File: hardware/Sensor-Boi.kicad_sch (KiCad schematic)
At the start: 3 parts, among them U1 ESP32-S3-WROOM-1, U2 MAX31856, U3 SN65HVD230

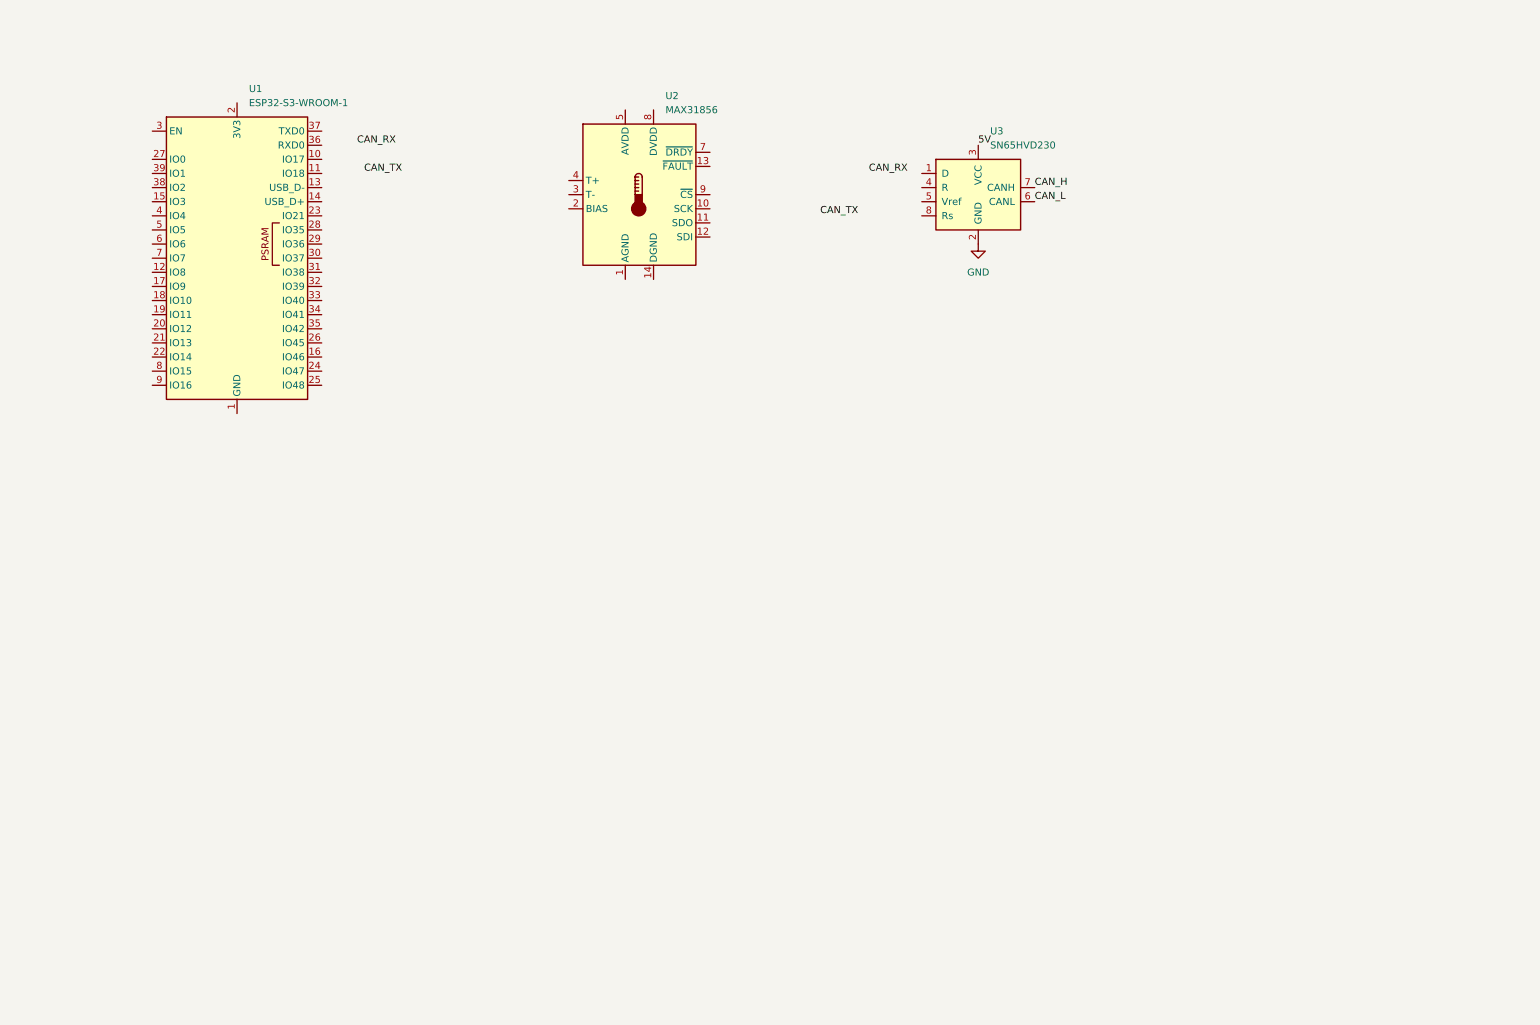
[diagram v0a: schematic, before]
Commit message: add a majority of symbols to schematic
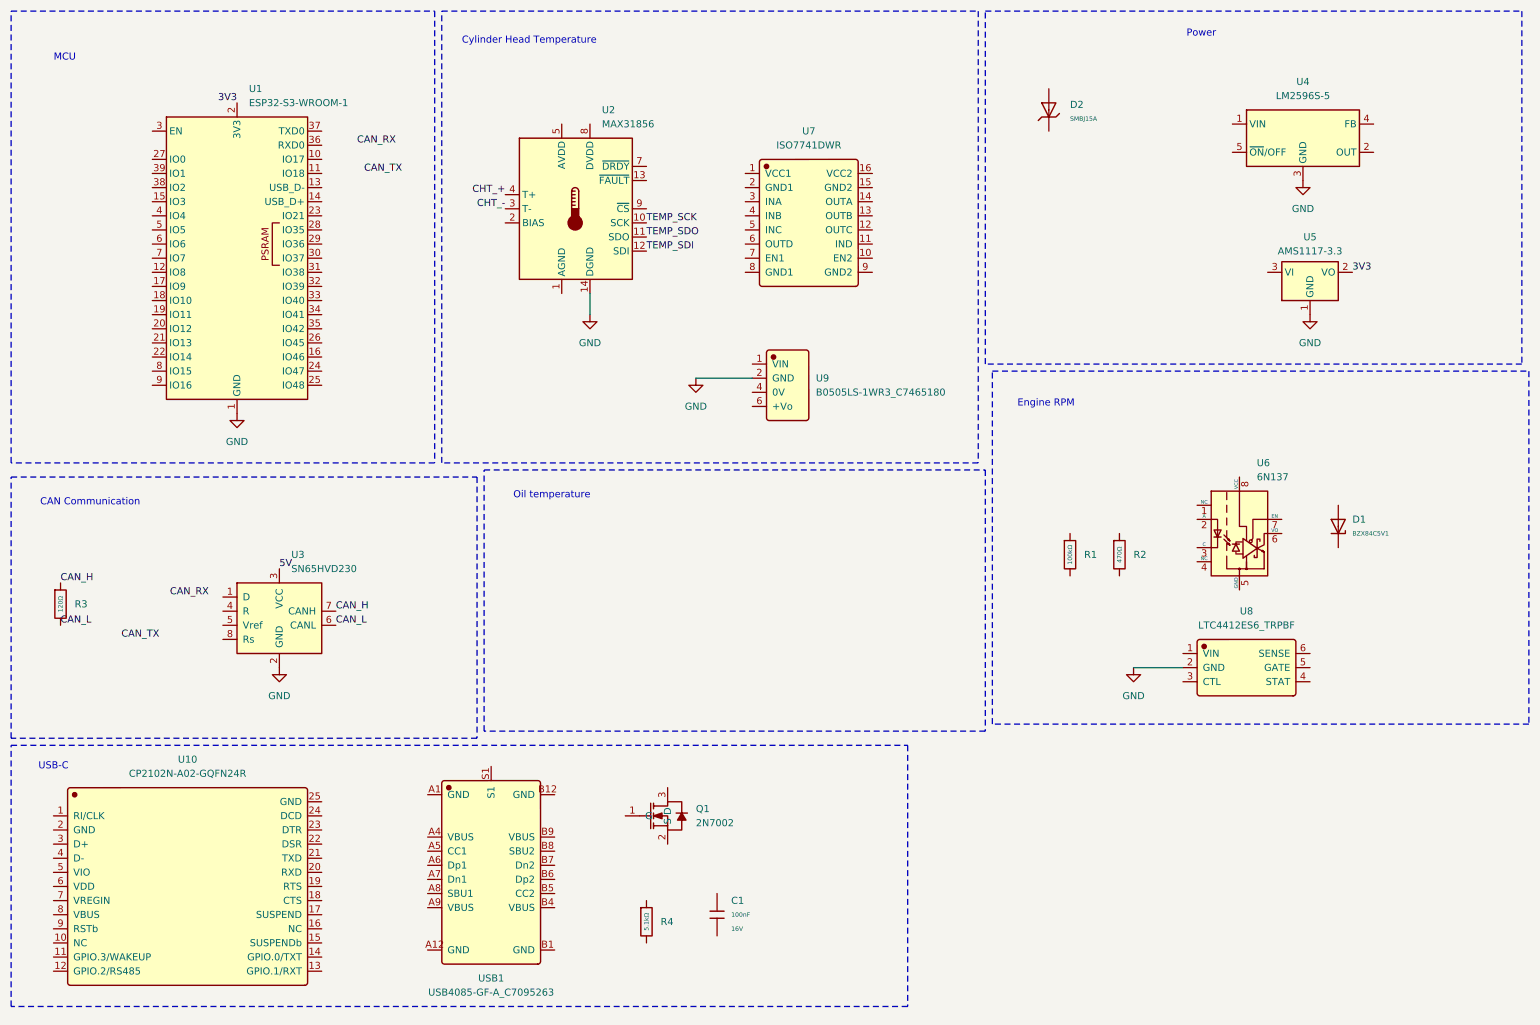
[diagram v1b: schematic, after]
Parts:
- added C1: 100nF, PCM_JLCPCB:C_0402, symbol PCM_JLCPCB-Capacitors:0402,100nF
- added D1: BZX84C5V1, PCM_JLCPCB:D_SOT-23, symbol PCM_JLCPCB-Diodes:Zener,BZX84C5V1
- added D2: SMBJ15A, PCM_JLCPCB:D_SMB, symbol PCM_JLCPCB-Diodes:TVS-Uni,SMBJ15A
- added Q1: 2N7002, Package_TO_SOT_SMD:SOT-23-3, symbol JLCImport:2N7002
- added R1: 100kΩ, PCM_JLCPCB:R_0402, symbol PCM_JLCPCB-Resistors:0402,100kΩ
- added R2: 470Ω, PCM_JLCPCB:R_0402, symbol PCM_JLCPCB-Resistors:0402,470Ω
- added R3: 120Ω, PCM_JLCPCB:R_0402, symbol PCM_JLCPCB-Resistors:0402,120Ω
- added R4: 5.1kΩ, PCM_JLCPCB:R_0402, symbol PCM_JLCPCB-Resistors:0402,5.1kΩ
- added U10: CP2102N-A02-GQFN24R, Package_DFN_QFN:QFN-28_4x4mm_P0.5mm, symbol JLCImport:CP2102N-A02-GQFN24R
- added U4: LM2596S-5, Package_TO_SOT_SMD:TO-263-5_TabPin3, symbol Regulator_Switching:LM2596S-5
- added U5: AMS1117-3.3, Package_TO_SOT_SMD:SOT-223-3_TabPin2, symbol Regulator_Linear:AMS1117-3.3
- added U6: 6N137, Package_DIP:DIP-8_W7.62mm, symbol Isolator:6N137
- added U7: ISO7741DWR, Package_SO:SOIC-16W_7.5x10.3mm_P1.27mm, symbol JLCImport:ISO7741DWR
- added U8: LTC4412ES6_TRPBF, PCM_JLCPCB:SOT-23-3_L2.9-W1.3-P0.95-LS2.4-BR, symbol JLCImport:LTC4412ES6_TRPBF
- added U9: B0505LS-1WR3_C7465180, JLCImport:B0505LS-1WR3_C7465180, symbol JLCImport:B0505LS-1WR3_C7465180
- added USB1: USB4085-GF-A_C7095263, Connector_USB:USB_C_Receptacle_GCT_USB4135-GF-A_6P_TopMnt_Horizontal, symbol JLCImport:USB4085-GF-A_C7095263
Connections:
- net CAN_H: now also R3.1
- net CAN_L: now also R3.2
- net GND: now also U1.1 (GND), U1.40 (GND), U1.41 (GND), U2.14 (DGND), U4.3 (GND), U5.1 (GND), U8.2 (GND), U9.2 (GND)
- net 3V3: now reaches U1.2 (3V3)
- net 3V3: now also U5.2 (VO)
- net TEMP_SCK: now reaches U2.10 (SCK)
- net TEMP_SDO: now reaches U2.11 (SDO)
- net TEMP_SDI: now reaches U2.12 (SDI)
- net CHT_-: now reaches U2.3 (T-)
- net CHT_+: now reaches U2.4 (T+)
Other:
- note added: "CAN Communication"
- note added: "Cylinder Head Temperature"
- note added: "Engine RPM"
- note added: "MCU"
- note added: "Oil temperature"
- note added: "Power"
- note added: "USB-C"
- moved on the sheet: U2, U3

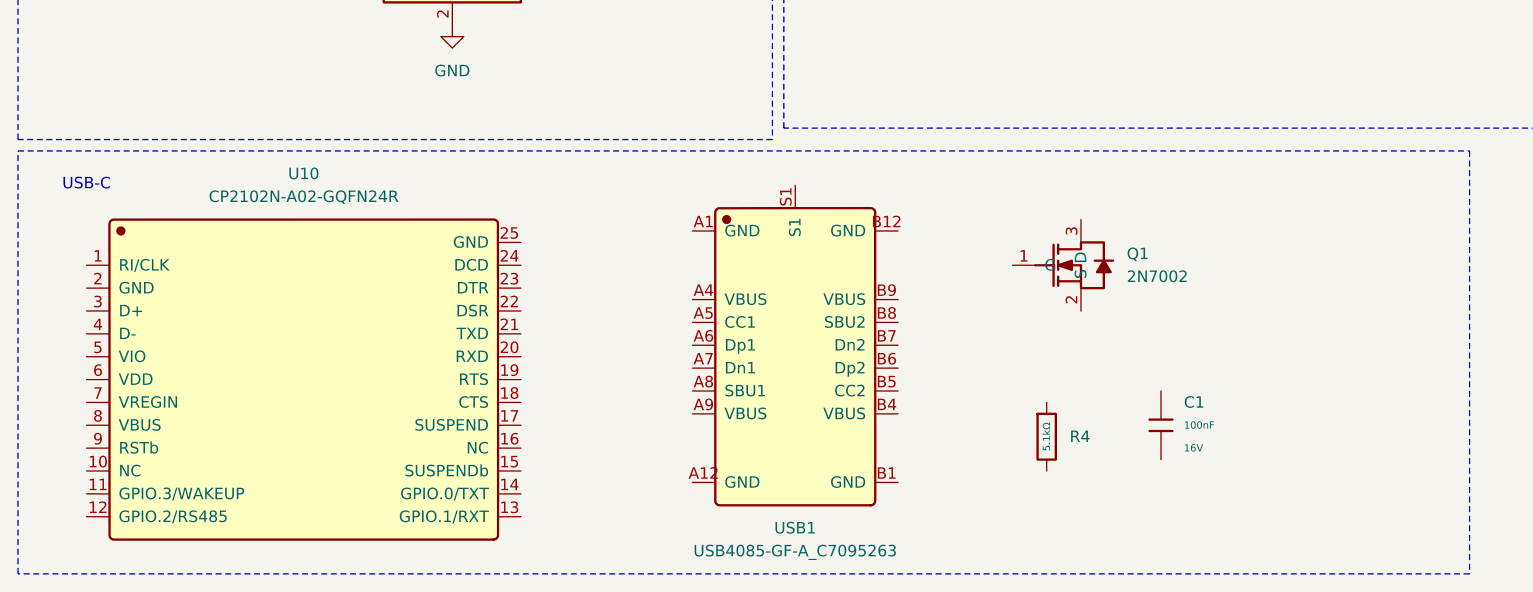
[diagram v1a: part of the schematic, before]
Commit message: add outline to pcb
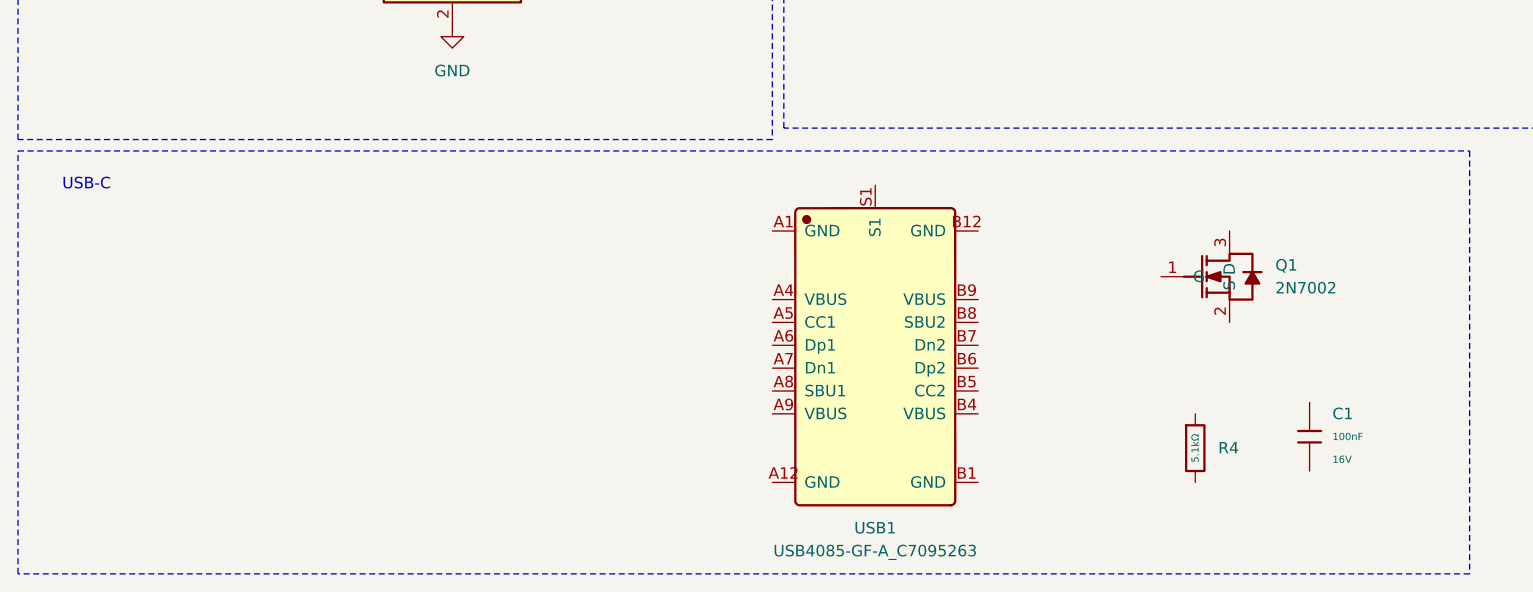
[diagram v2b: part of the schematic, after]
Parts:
- removed U10: CP2102N-A02-GQFN24R, Package_DFN_QFN:QFN-28_4x4mm_P0.5mm, symbol JLCImport:CP2102N-A02-GQFN24R
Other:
- moved on the sheet: C1, Q1, R4, USB1

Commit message: add some connections
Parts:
- added C2: 100nF, PCM_JLCPCB:C_0402, symbol PCM_JLCPCB-Capacitors:0402,100nF
- added R5: 100Ω, PCM_JLCPCB:R_0402, symbol PCM_JLCPCB-Resistors:0402,100kΩ
- added R6: 10kΩ, PCM_JLCPCB:R_0402, symbol PCM_JLCPCB-Resistors:0402,100kΩ
- added R7: 15kΩ, PCM_JLCPCB:R_0402, symbol PCM_JLCPCB-Resistors:0402,100kΩ
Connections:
- net CAN_RX: now also U1.10 (IO17)
- net CAN_TX: now also U1.11 (IO18)
- net GND: now also C2.2, R7.2
- net USB_D-: now reaches U1.13 (USB_D-)
- net USB_D+: now reaches U1.14 (USB_D+)
- net PB_Bat_MCU: now reaches U1.15 (IO3)
- net OIL_MCU: now reaches U1.38 (IO2)
- net Lambda_MCU: now reaches U1.6 (IO6)
- net Lambda_MCU: now also C2.1, R6.2, R7.1
- new net: R5.2, R6.1
- new net Lambda_In: R5.1
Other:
- moved on the sheet: C1, Q1, R4, USB1

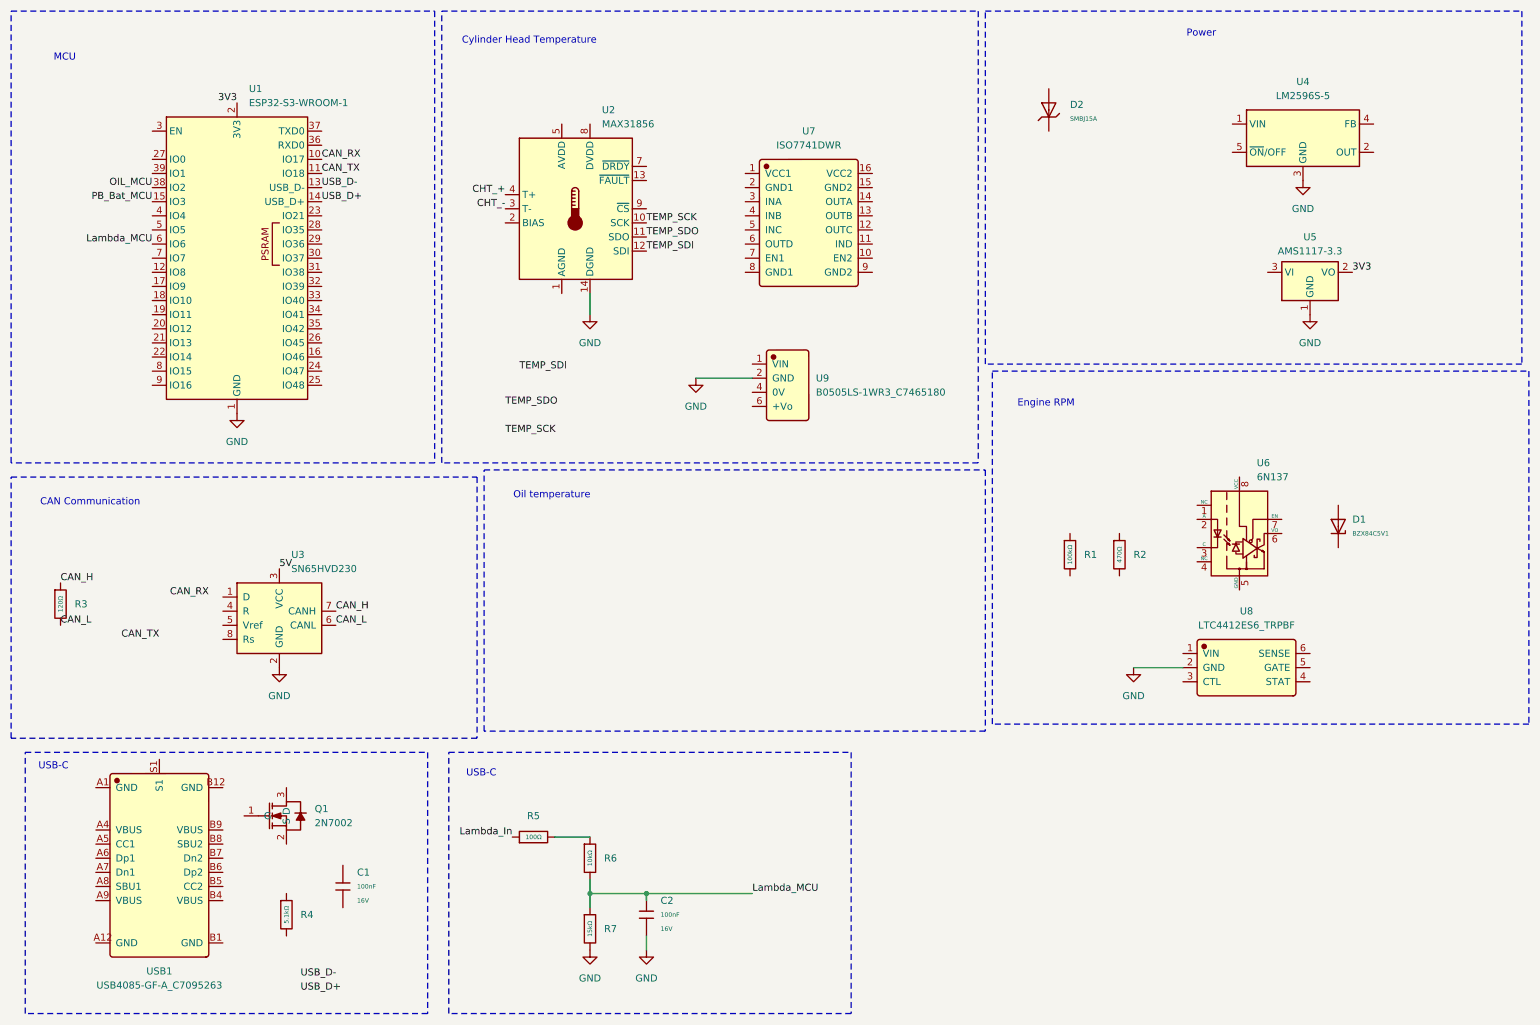
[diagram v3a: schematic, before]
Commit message: add power electronics and connections
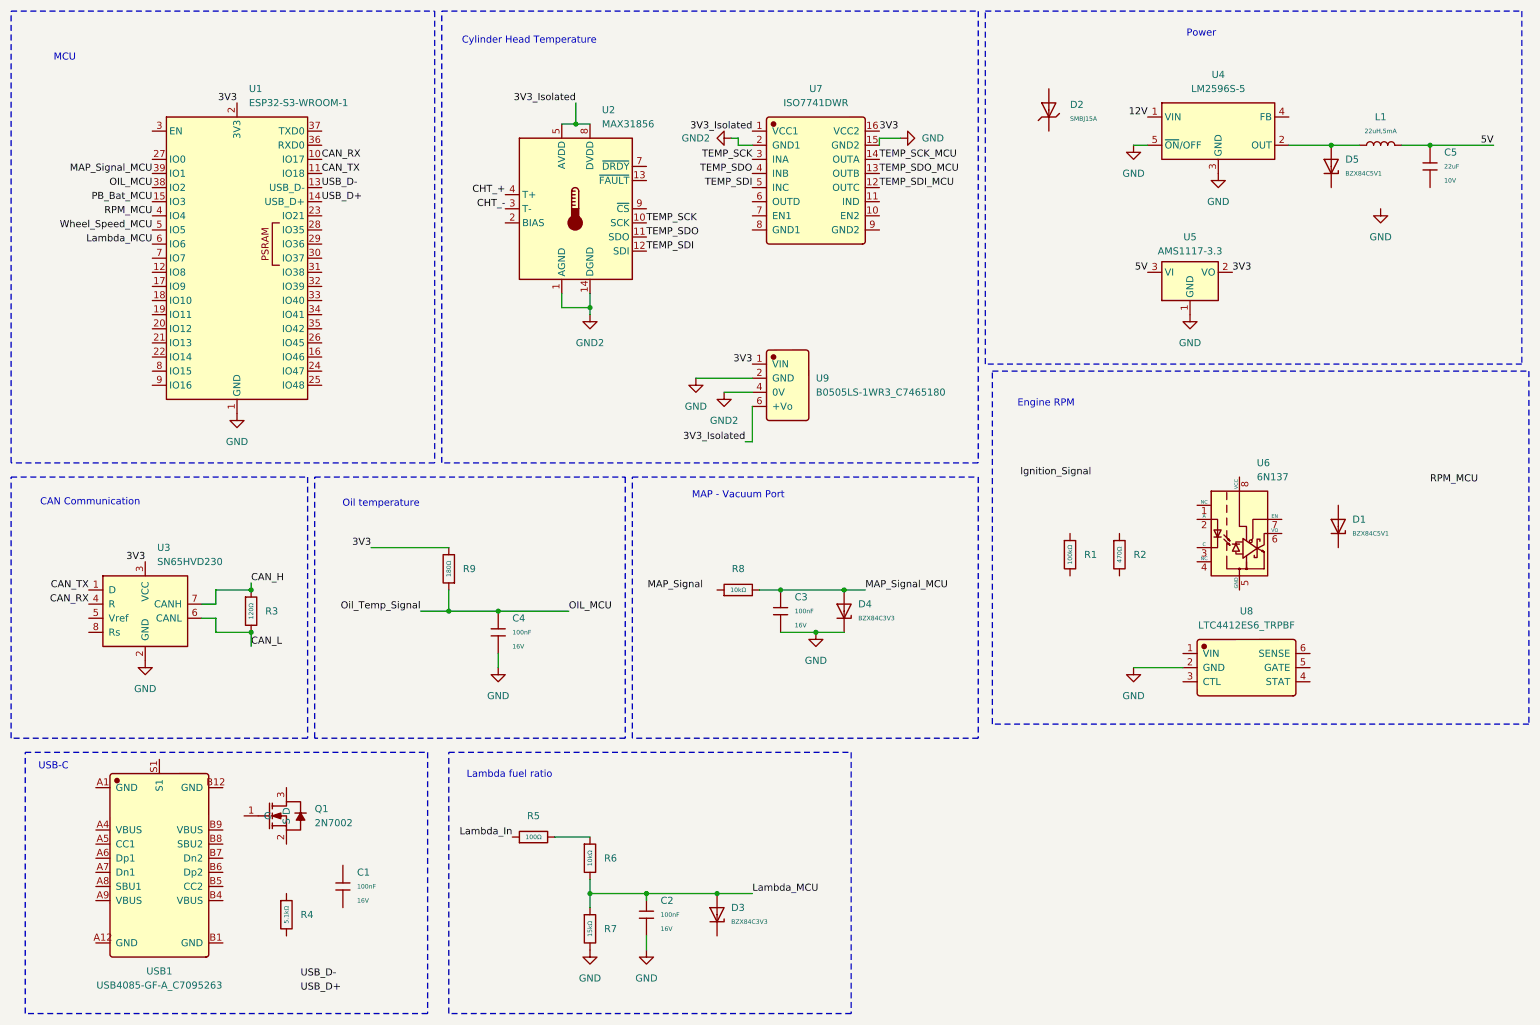
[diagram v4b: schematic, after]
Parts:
- added C3, C4: 100nF, PCM_JLCPCB:C_0402, symbol PCM_JLCPCB-Capacitors:0402,100nF
- added C5: 22uF, PCM_JLCPCB:C_1206, symbol PCM_JLCPCB-Capacitors:1206,22uF
- added D3, D4: BZX84C3V3, PCM_JLCPCB:D_SOT-23, symbol PCM_JLCPCB-Diodes:Zener,BZX84C3V3
- added D5: BZX84C5V1, PCM_JLCPCB:D_SOT-23, symbol PCM_JLCPCB-Diodes:Zener,BZX84C5V1
- added L1: 22uH,5mA, PCM_JLCPCB:L_0805, symbol PCM_JLCPCB-Inductors:22uH,5mA
- added R8: 10kΩ, PCM_JLCPCB:R_0402, symbol PCM_JLCPCB-Resistors:0402,100kΩ
- added R9: 180Ω, PCM_JLCPCB:R_0402, symbol PCM_JLCPCB-Resistors:0402,100kΩ
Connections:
- net 3V3: now also U3.3 (VCC), U7.16 (VCC2), U9.1 (VIN), R9.2
- net 5V: now also U5.3 (VI), C5.1, L1.2; no longer U3.3 (VCC)
- net CAN_RX: now also U3.4 (R)
- net CAN_TX: now also U3.1 (D)
- net GND: now also U4.5 (~{ON}/OFF), U7.15 (GND2), C3.2, C4.2, D4.3; no longer U2.14 (DGND)
- net Lambda_MCU: now also D3.1
- net OIL_MCU: now also C4.1, R9.1
- net TEMP_SCK: now also U7.3 (INA)
- net TEMP_SDI: now also U7.5 (INC)
- net TEMP_SDO: now also U7.4 (INB)
- net MAP_Signal_MCU: now reaches U1.39 (IO1)
- net MAP_Signal_MCU: now also C3.1, D4.1, R8.2
- net RPM_MCU: now reaches U1.4 (IO4)
- net Wheel_Speed_MCU: now reaches U1.5 (IO5)
- net 12V: now reaches U4.1 (VIN)
- net at U4.2 (OUT): now also D5.1, L1.1
- net 3V3_Isolated: now reaches U7.1 (VCC1)
- net 3V3_Isolated: now also U2.5 (AVDD), U2.8 (DVDD), U9.6 (+Vo)
- net TEMP_SDI_MCU: now reaches U7.12 (OUTC)
- net TEMP_SDO_MCU: now reaches U7.13 (OUTB)
- net TEMP_SCK_MCU: now reaches U7.14 (OUTA)
- net GND2: now reaches U7.2 (GND1)
- net GND2: now also U2.1 (AGND), U2.14 (DGND), U9.4 (0V)
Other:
- note added: "Lambda fuel ratio"
- note added: "MAP - Vacuum Port"
- moved on the sheet: R3, U3, U4, U5, U7
